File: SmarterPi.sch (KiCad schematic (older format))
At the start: 12 parts, among them J1 Raspberry_Pi_2_3, J2 RJ10, J3 Screw_Terminal_01x04, J4 Screw_Terminal_01x03

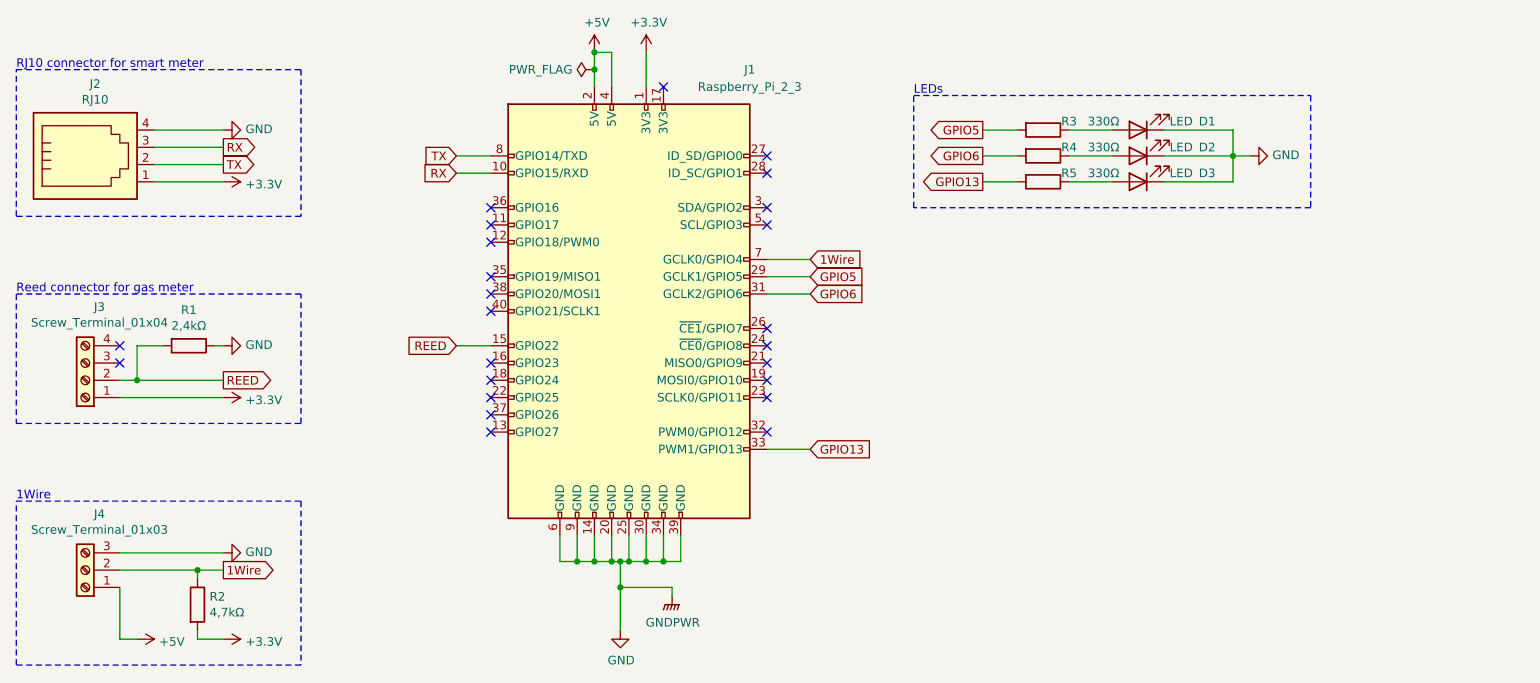
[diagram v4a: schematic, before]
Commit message: Added 3 push buttons
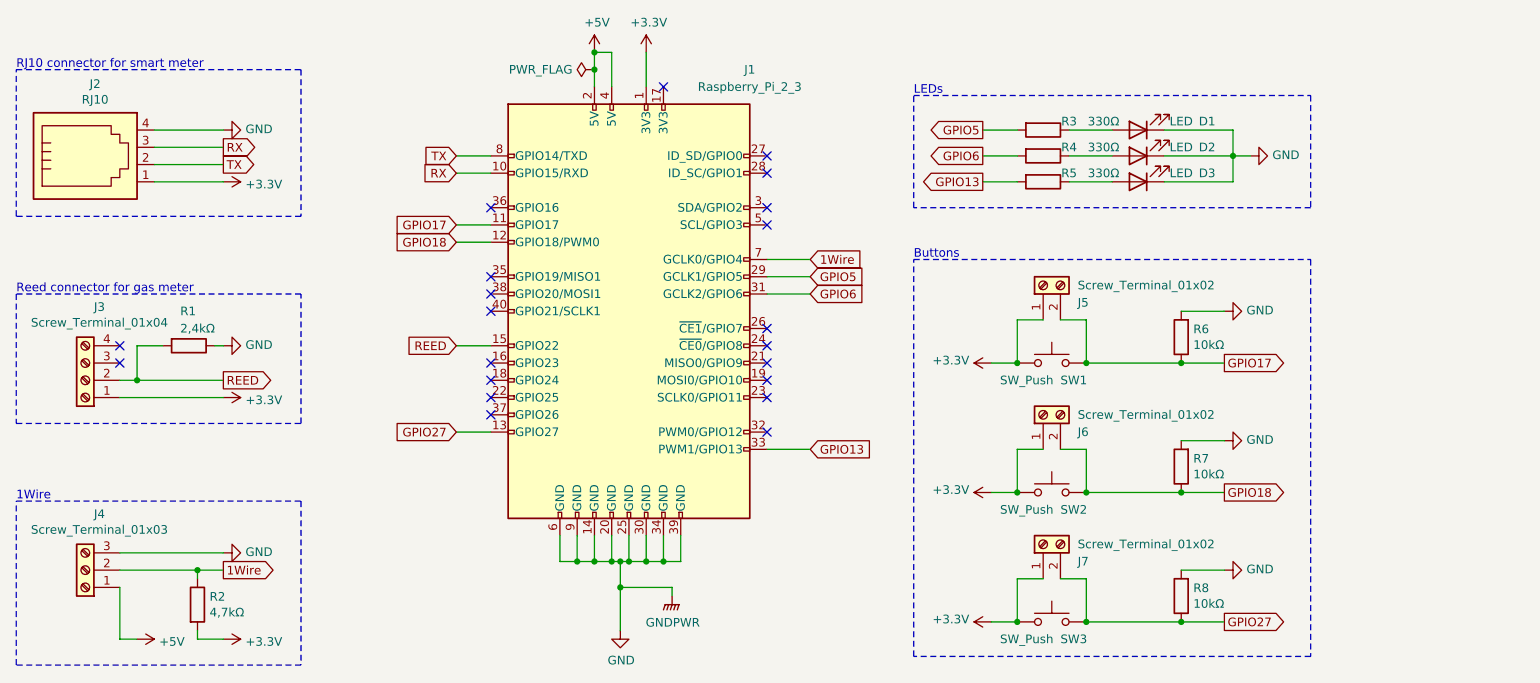
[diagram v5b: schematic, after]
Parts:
- added J5, J6, J7: Screw_Terminal_01x02, TerminalBlock:TerminalBlock_bornier-2_P5.08mm, symbol Connector:Screw_Terminal_01x02
- added R6, R7, R8: 10kΩ, Resistor_SMD:R_0805_2012Metric_Pad1.20x1.40mm_HandSolder, symbol Device:R
- added SW1, SW2, SW3: SW_Push, Button_Switch_SMD:SW_SPST_CK_RS282G05A3, symbol Switch:SW_Push
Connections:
- net +3V3: now also J5.1 (Pin_1), J6.1 (Pin_1), J7.1 (Pin_1), SW1.1, SW2.1, SW3.1
- net GND: now also R6.2, R7.2, R8.2
- net GPIO17: now reaches J1.11 (GPIO17)
- net GPIO17: now also J5.2 (Pin_2), R6.1, SW1.2
- net GPIO18: now reaches J1.12 (GPIO18/PWM0)
- net GPIO18: now also J6.2 (Pin_2), R7.1, SW2.2
- net GPIO27: now reaches J1.13 (GPIO27)
- net GPIO27: now also J7.2 (Pin_2), R8.1, SW3.2
- no-connect marks 24 -> 21
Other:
- note added: "Buttons"

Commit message: Minor fixes
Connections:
- net GND: no longer J1.6 (GND)
- no-connect marks 21 -> 22
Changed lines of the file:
@@
 $EndComp
-Wire Wire Line
-	5300 5050 5300 5200
-Wire Wire Line
-	5300 5200 5400 5200
 Wire Wire Line
 	6000 5050 6000 5200
@@
 Wire Wire Line
 	5400 5050 5400 5200
-Connection ~ 5400 5200
 Wire Wire Line
 	5400 5200 5500 5200
@@
 Text Notes 7350 3450 0    50   ~ 0
 Buttons
+NoConn ~ 5300 5050
 $EndSCHEMATC

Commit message: 0.1
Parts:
- R1: value 2,4kΩ -> 2,2kΩ
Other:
- note added: "B"
- note added: "G"
- note added: "W"
- note added: "Y"
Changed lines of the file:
@@
 P 3150 3950
 F 0 "R1" V 2950 3900 50  0000 L CNN
-F 1 "2,4kΩ" V 3050 3900 50  0000 L CNN
+F 1 "2,2kΩ" V 3050 3900 50  0000 L CNN
 F 2 "Resistor_THT:R_Axial_DIN0207_L6.3mm_D2.5mm_P10.16mm_Horizontal" V 3080 3950 50  0001 C CNN
 F 3 "~" H 3150 3950 50  0001 C CNN
@@
 Buttons
 NoConn ~ 5300 5050
+Text Notes 2450 4250 1    50   ~ 0
+G
+Text Notes 2450 4150 1    50   ~ 0
+B
+Text Notes 2450 4050 1    50   ~ 0
+W
+Text Notes 2450 3950 1    50   ~ 0
+Y
 $EndSCHEMATC

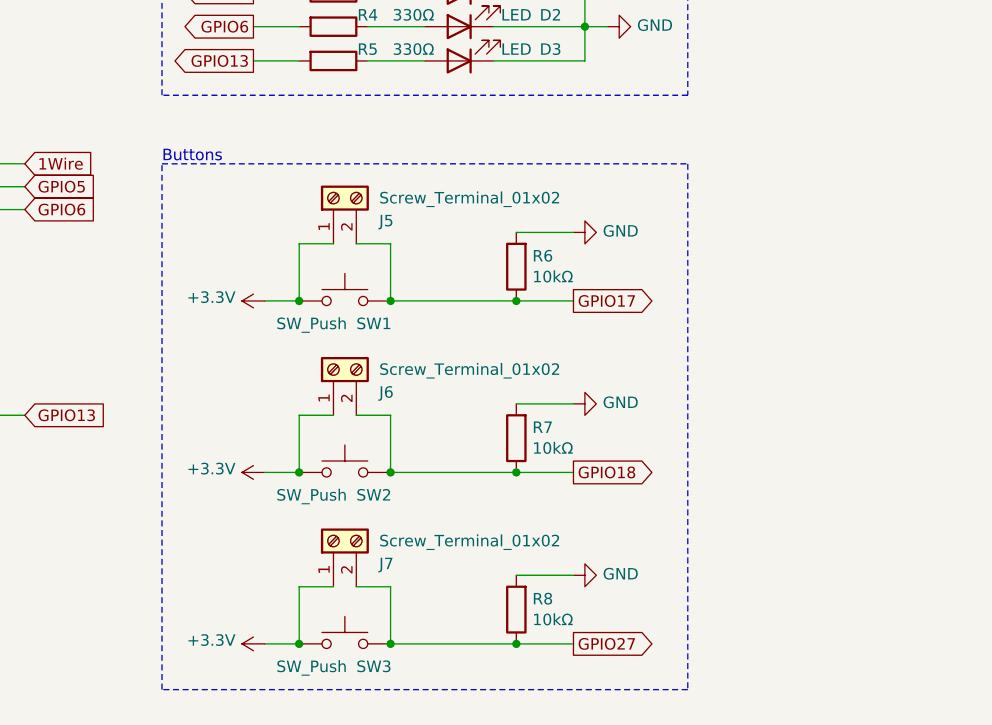
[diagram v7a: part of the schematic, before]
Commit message: Smaller terminal block for buttons
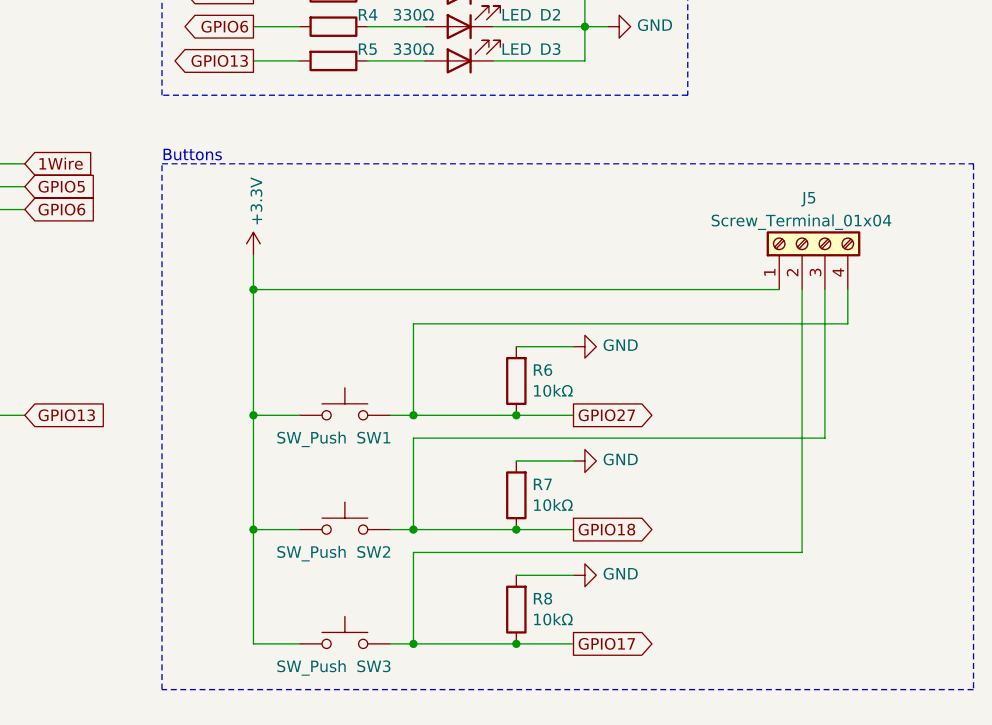
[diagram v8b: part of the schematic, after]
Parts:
- removed J5, J6, J7: Screw_Terminal_01x02, TerminalBlock:TerminalBlock_bornier-2_P5.08mm, symbol Connector:Screw_Terminal_01x02
- added J5: Screw_Terminal_01x04, TerminalBlock_Phoenix:TerminalBlock_Phoenix_MPT-0,5-4-2.54_1x04_P2.54mm_Horizontal, symbol Connector:Screw_Terminal_01x04
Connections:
- net +3V3: now also J5.1 (Pin_1)
- net GPIO17: now also R8.1, SW3.2, J5.2 (Pin_2); no longer R6.1, SW1.2
- net GPIO18: now also J5.3 (Pin_3)
- net GPIO27: now also R6.1, SW1.2, J5.4 (Pin_4); no longer R8.1, SW3.2
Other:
- moved on the sheet: R6, R7, SW1, SW2
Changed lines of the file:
@@
 Sheet 1 1
 Title "Smarter Pi"
-Date "2021-02-19"
-Rev "0.1"
+Date "2021-10-21"
+Rev "0.2"
 Comp "haus-automatisierung.com"
 Comment1 "Matthias Kleine"
@@
 Wire Wire Line
 	4700 3250 4900 3250
-Text GLabel 9150 4050 2    50   Output ~ 0
-GPIO17
+Text GLabel 9150 4550 2    50   Output ~ 0
+GPIO27
 $Comp
 L Switch:SW_Push SW1
 U 1 1 6030C6F8
-P 8150 4050
-F 0 "SW1" H 8200 3950 50  0000 L CNN
-F 1 "SW_Push" H 7850 3950 50  0000 L CNN
-F 2 "Button_Switch_SMD:SW_SPST_CK_RS282G05A3" H 8150 4250 50  0001 C CNN
-F 3 "~" H 8150 4250 50  0001 C CNN
-	1    8150 4050
-	1    0    0    -1
-$EndComp
-$Comp
-L Connector:Screw_Terminal_01x02 J5
-U 1 1 6030E42A
-P 8100 3600
-F 0 "J5" V 8000 3400 50  0000 R CNN
-F 1 "Screw_Terminal_01x02" V 8100 3400 50  0000 R CNN
-F 2 "TerminalBlock:TerminalBlock_bornier-2_P5.08mm" H 8100 3600 50  0001 C CNN
-F 3 "~" H 8100 3600 50  0001 C CNN
-	1    8100 3600
-	0    -1   -1   0
+P 8150 4550
+F 0 "SW1" H 8200 4450 50  0000 L CNN
+F 1 "SW_Push" H 7850 4450 50  0000 L CNN
+F 2 "Button_Switch_SMD:SW_SPST_CK_RS282G05A3" H 8150 4750 50  0001 C CNN
+F 3 "~" H 8150 4750 50  0001 C CNN
+	1    8150 4550
+	1    0    0    -1
 $EndComp
 $Comp
 L Device:R R6
 U 1 1 603133E9
-P 8900 3900
-F 0 "R6" H 8830 3854 50  0000 R CNN
-F 1 "10kΩ" H 8830 3945 50  0000 R CNN
-F 2 "Resistor_SMD:R_0805_2012Metric_Pad1.20x1.40mm_HandSolder" V 8830 3900 50  0001 C CNN
-F 3 "~" H 8900 3900 50  0001 C CNN
-	1    8900 3900
+P 8900 4400
+F 0 "R6" H 8830 4354 50  0000 R CNN
+F 1 "10kΩ" H 8830 4445 50  0000 R CNN
+F 2 "Resistor_SMD:R_0805_2012Metric_Pad1.20x1.40mm_HandSolder" V 8830 4400 50  0001 C CNN
+F 3 "~" H 8900 4400 50  0001 C CNN
+	1    8900 4400
 	-1   0    0    1
 $EndComp
 Wire Wire Line
-	7950 4050 7950 3800
-Wire Wire Line
-	7950 3800 8100 3800
-Wire Wire Line
-	8350 4050 8350 3800
-Wire Wire Line
-	8350 3800 8200 3800
-Wire Wire Line
-	8350 4050 8900 4050
-Connection ~ 8350 4050
-Connection ~ 8900 4050
-Wire Wire Line
-	8900 4050 9150 4050
+	8350 4550 8450 4550
+Connection ~ 8900 4550
+Wire Wire Line
+	8900 4550 9150 4550
 $Comp
 L power:GND #PWR016
 U 1 1 60332B83
-P 9150 3750
-F 0 "#PWR016" H 9150 3500 50  0001 C CNN
-F 1 "GND" V 9155 3622 50  0000 R CNN
-F 2 "" H 9150 3750 50  0001 C CNN
-F 3 "" H 9150 3750 50  0001 C CNN
-	1    9150 3750
-	0    -1   -1   0
-$EndComp
-Wire Wire Line
-	9150 3750 8900 3750
-$Comp
-L power:+3.3V #PWR013
-U 1 1 60335572
-P 7800 4050
-F 0 "#PWR013" H 7800 3900 50  0001 C CNN
-F 1 "+3.3V" V 7815 4178 50  0000 L CNN
-F 2 "" H 7800 4050 50  0001 C CNN
-F 3 "" H 7800 4050 50  0001 C CNN
-	1    7800 4050
-	0    -1   -1   0
-$EndComp
-Wire Wire Line
-	7800 4050 7950 4050
-Connection ~ 7950 4050
-Text GLabel 9150 4800 2    50   Output ~ 0
+P 9150 4250
+F 0 "#PWR016" H 9150 4000 50  0001 C CNN
+F 1 "GND" V 9155 4122 50  0000 R CNN
+F 2 "" H 9150 4250 50  0001 C CNN
+F 3 "" H 9150 4250 50  0001 C CNN
+	1    9150 4250
+	0    -1   -1   0
+$EndComp
+Wire Wire Line
+	9150 4250 8900 4250
+Text GLabel 9150 5050 2    50   Output ~ 0
 GPIO18
 $Comp
 L Switch:SW_Push SW2
 U 1 1 603494F2
-P 8150 4800
-F 0 "SW2" H 8200 4700 50  0000 L CNN
-F 1 "SW_Push" H 7850 4700 50  0000 L CNN
-F 2 "Button_Switch_SMD:SW_SPST_CK_RS282G05A3" H 8150 5000 50  0001 C CNN
-F 3 "~" H 8150 5000 50  0001 C CNN
-	1    8150 4800
-	1    0    0    -1
-$EndComp
-$Comp
-L Connector:Screw_Terminal_01x02 J6
-U 1 1 603494F8
-P 8100 4350
-F 0 "J6" V 8000 4150 50  0000 R CNN
-F 1 "Screw_Terminal_01x02" V 8100 4150 50  0000 R CNN
-F 2 "TerminalBlock:TerminalBlock_bornier-2_P5.08mm" H 8100 4350 50  0001 C CNN
-F 3 "~" H 8100 4350 50  0001 C CNN
-	1    8100 4350
-	0    -1   -1   0
+P 8150 5050
+F 0 "SW2" H 8200 4950 50  0000 L CNN
+F 1 "SW_Push" H 7850 4950 50  0000 L CNN
+F 2 "Button_Switch_SMD:SW_SPST_CK_RS282G05A3" H 8150 5250 50  0001 C CNN
+F 3 "~" H 8150 5250 50  0001 C CNN
+	1    8150 5050
+	1    0    0    -1
 $EndComp
 $Comp
 L Device:R R7
 U 1 1 603494FE
-P 8900 4650
-F 0 "R7" H 8830 4604 50  0000 R CNN
-F 1 "10kΩ" H 8830 4695 50  0000 R CNN
-F 2 "Resistor_SMD:R_0805_2012Metric_Pad1.20x1.40mm_HandSolder" V 8830 4650 50  0001 C CNN
-F 3 "~" H 8900 4650 50  0001 C CNN
-	1    8900 4650
+P 8900 4900
+F 0 "R7" H 8830 4854 50  0000 R CNN
+F 1 "10kΩ" H 8830 4945 50  0000 R CNN
+F 2 "Resistor_SMD:R_0805_2012Metric_Pad1.20x1.40mm_HandSolder" V 8830 4900 50  0001 C CNN
+F 3 "~" H 8900 4900 50  0001 C CNN
+	1    8900 4900
 	-1   0    0    1
 $EndComp
 Wire Wire Line
-	7950 4800 7950 4550
-Wire Wire Line
-	7950 4550 8100 4550
-Wire Wire Line
-	8350 4800 8350 4550
-Wire Wire Line
-	8350 4550 8200 4550
-Wire Wire Line
-	8350 4800 8900 4800
-Connection ~ 8350 4800
-Connection ~ 8900 4800
-Wire Wire Line
-	8900 4800 9150 4800
+	8350 5050 8450 5050
+Connection ~ 8900 5050
+Wire Wire Line
+	8900 5050 9150 5050
 $Comp
 L power:GND #PWR017
 U 1 1 6034950C
-P 9150 4500
-F 0 "#PWR017" H 9150 4250 50  0001 C CNN
-F 1 "GND" V 9155 4372 50  0000 R CNN
-F 2 "" H 9150 4500 50  0001 C CNN
-F 3 "" H 9150 4500 50  0001 C CNN
-	1    9150 4500
-	0    -1   -1   0
-$EndComp
-Wire Wire Line
-	9150 4500 8900 4500
-$Comp
-L power:+3.3V #PWR014
-U 1 1 60349513
-P 7800 4800
-F 0 "#PWR014" H 7800 4650 50  0001 C CNN
-F 1 "+3.3V" V 7815 4928 50  0000 L CNN
-F 2 "" H 7800 4800 50  0001 C CNN
-F 3 "" H 7800 4800 50  0001 C CNN
-	1    7800 4800
-	0    -1   -1   0
-$EndComp
-Wire Wire Line
-	7800 4800 7950 4800
-Connection ~ 7950 4800
+P 9150 4750
+F 0 "#PWR017" H 9150 4500 50  0001 C CNN
+F 1 "GND" V 9155 4622 50  0000 R CNN
+F 2 "" H 9150 4750 50  0001 C CNN
+F 3 "" H 9150 4750 50  0001 C CNN
+	1    9150 4750
+	0    -1   -1   0
+$EndComp
+Wire Wire Line
+	9150 4750 8900 4750
 Text GLabel 9150 5550 2    50   Output ~ 0
-GPIO27
+GPIO17
 $Comp
 L Switch:SW_Push SW3
@@
 	1    8150 5550
 	1    0    0    -1
-$EndComp
-$Comp
-L Connector:Screw_Terminal_01x02 J7
-U 1 1 6034E172
-P 8100 5100
-F 0 "J7" V 8000 4900 50  0000 R CNN
-F 1 "Screw_Terminal_01x02" V 8100 4900 50  0000 R CNN
-F 2 "TerminalBlock:TerminalBlock_bornier-2_P5.08mm" H 8100 5100 50  0001 C CNN
-F 3 "~" H 8100 5100 50  0001 C CNN
-	1    8100 5100
-	0    -1   -1   0
 $EndComp
 $Comp
@@
 $EndComp
 Wire Wire Line
-	7950 5550 7950 5300
-Wire Wire Line
-	7950 5300 8100 5300
-Wire Wire Line
-	8350 5550 8350 5300
-Wire Wire Line
-	8350 5300 8200 5300
-Wire Wire Line
-	8350 5550 8900 5550
-Connection ~ 8350 5550
+	8350 5550 8450 5550
 Connection ~ 8900 5550
 Wire Wire Line
@@
 Wire Wire Line
 	9150 5250 8900 5250
-$Comp
-L power:+3.3V #PWR015
-U 1 1 6034E18D
-P 7800 5550
-F 0 "#PWR015" H 7800 5400 50  0001 C CNN
-F 1 "+3.3V" V 7815 5678 50  0000 L CNN
-F 2 "" H 7800 5550 50  0001 C CNN
-F 3 "" H 7800 5550 50  0001 C CNN
-	1    7800 5550
-	0    -1   -1   0
-$EndComp
-Wire Wire Line
-	7800 5550 7950 5550
-Connection ~ 7950 5550
-Wire Notes Line
-	7350 3450 9650 3450
-Wire Notes Line
-	9650 3450 9650 5750
-Wire Notes Line
-	9650 5750 7350 5750
+Wire Notes Line
+	7350 3450 10900 3450
+Wire Notes Line
+	10900 3450 10900 5750
+Wire Notes Line
+	10900 5750 7350 5750
 Wire Notes Line
 	7350 5750 7350 3450
@@
 Text Notes 2450 3950 1    50   ~ 0
 Y
+$Comp
+L power:+3.3V #PWR013
+U 1 1 60335572
+P 7750 3850
+F 0 "#PWR013" H 7750 3700 50  0001 C CNN
+F 1 "+3.3V" V 7765 3978 50  0000 L CNN
+F 2 "" H 7750 3850 50  0001 C CNN
+F 3 "" H 7750 3850 50  0001 C CNN
+	1    7750 3850
+	1    0    0    -1
+$EndComp
+Wire Wire Line
+	7750 3850 7750 4000
+Wire Wire Line
+	7750 5550 7950 5550
+Wire Wire Line
+	7950 4550 7750 4550
+Connection ~ 7750 4550
+Wire Wire Line
+	7750 4550 7750 5050
+Wire Wire Line
+	7950 5050 7750 5050
+Connection ~ 7750 5050
+Wire Wire Line
+	7750 5050 7750 5550
+Wire Wire Line
+	7750 4000 10050 4000
+Connection ~ 7750 4000
+Wire Wire Line
+	7750 4000 7750 4550
+Wire Wire Line
+	8450 4150 8450 4550
+Connection ~ 8450 4550
+Wire Wire Line
+	8450 4550 8900 4550
+Wire Wire Line
+	10250 4000 10250 4650
+Wire Wire Line
+	10250 4650 8450 4650
+Wire Wire Line
+	8450 4650 8450 5050
+Connection ~ 8450 5050
+Wire Wire Line
+	8450 5050 8900 5050
+Wire Wire Line
+	8450 5150 8450 5550
+Connection ~ 8450 5550
+Wire Wire Line
+	8450 5550 8900 5550
+$Comp
+L Connector:Screw_Terminal_01x04 J5
+U 1 1 61756B46
+P 10150 3800
+F 0 "J5" V 10350 3800 50  0000 R CNN
+F 1 "Screw_Terminal_01x04" V 10250 4200 50  0000 R CNN
+F 2 "TerminalBlock_Phoenix:TerminalBlock_Phoenix_MPT-0,5-4-2.54_1x04_P2.54mm_Horizontal" H 10150 3800 50  0001 C CNN
+F 3 "~" H 10150 3800 50  0001 C CNN
+	1    10150 3800
+	0    -1   -1   0
+$EndComp
+Wire Wire Line
+	8450 4150 10350 4150
+Wire Wire Line
+	10350 4150 10350 4000
+Wire Wire Line
+	8450 5150 10150 5150
+Wire Wire Line
+	10150 5150 10150 4000
 $EndSCHEMATC
